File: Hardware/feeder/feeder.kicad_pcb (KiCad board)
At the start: 2 copper layers, 8 parts, among them J1 Conn_01x02, Q1 BUZ11

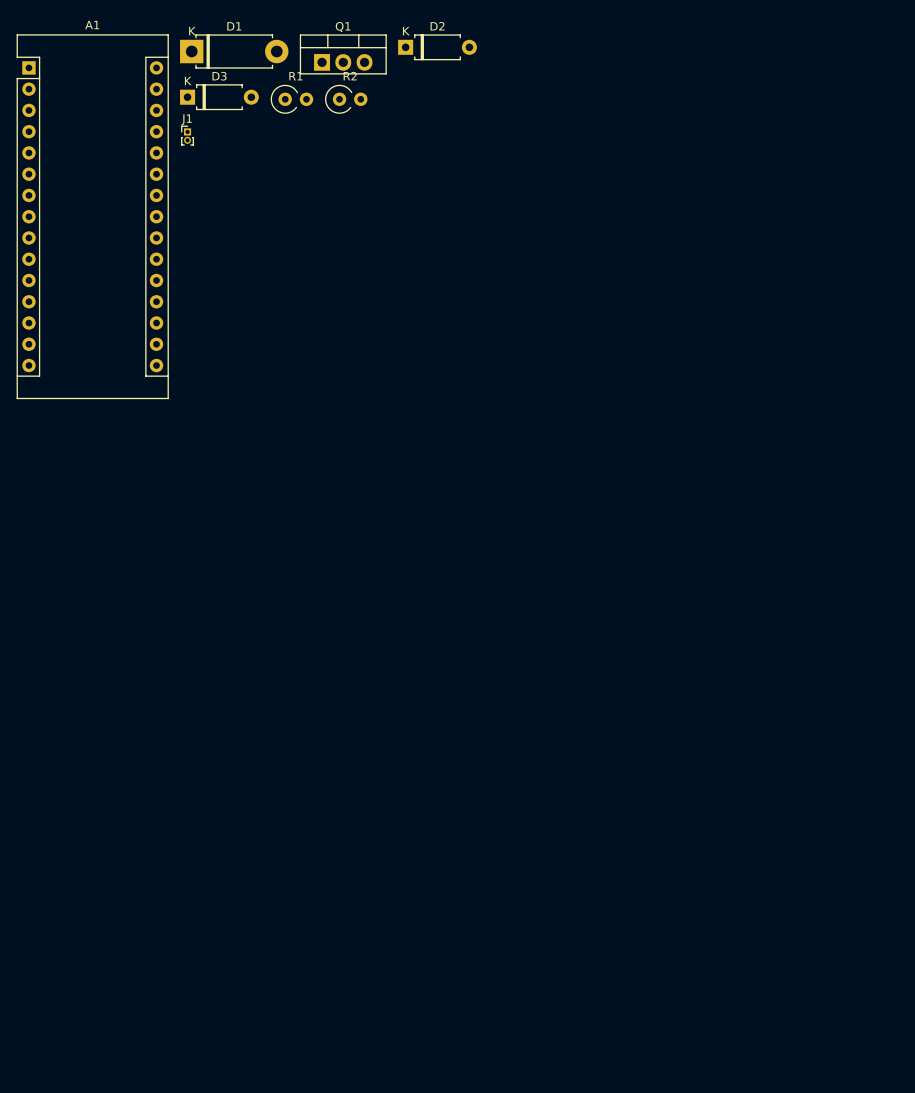
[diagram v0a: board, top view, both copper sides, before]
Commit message: Updated hardware schematics and layout
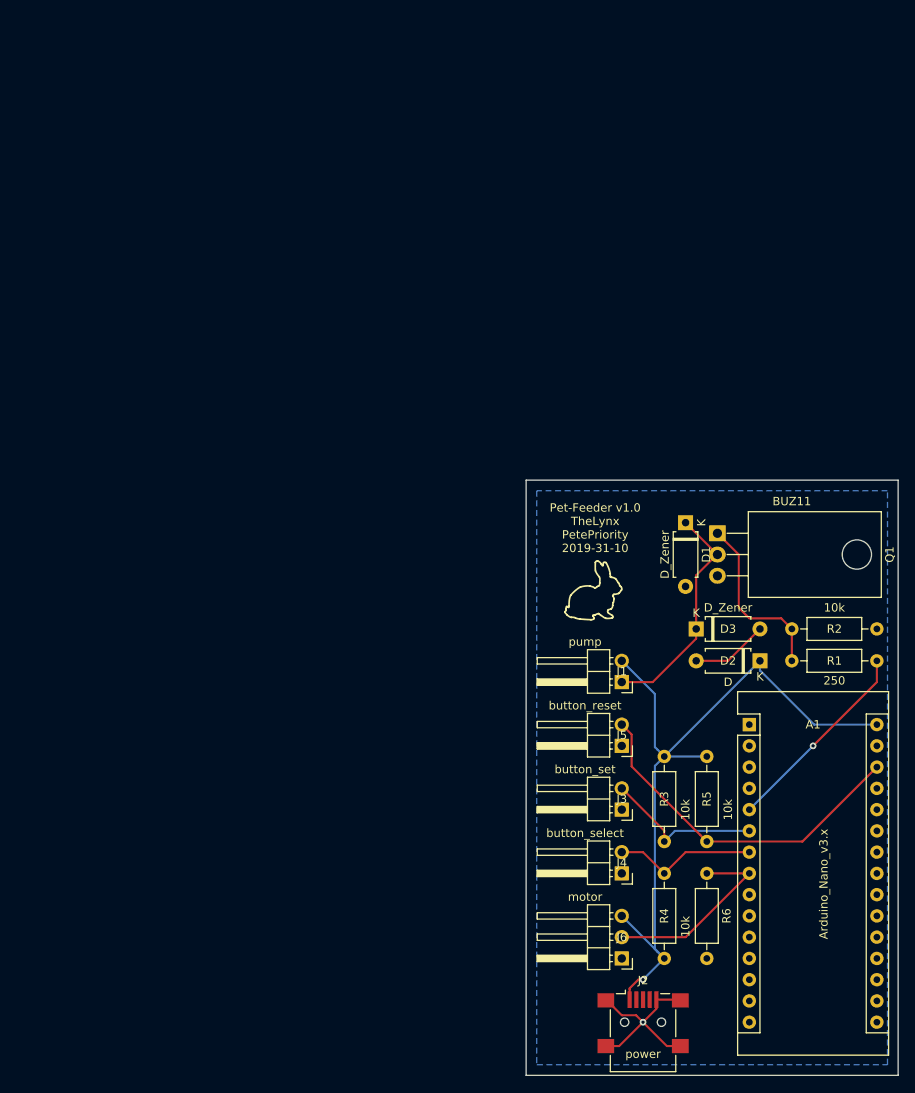
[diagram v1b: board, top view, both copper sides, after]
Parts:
- added J2: power, Connector_USB:USB_Mini-B_Lumberg_2486_01_Horizontal, F.Cu at (127.0, 141.0)
- added J3: button_set, Connector_PinHeader_2.54mm:PinHeader_1x02_P2.54mm_Horizontal, F.Cu at (124.5, 115.6)
- added J4: button_select, Connector_PinHeader_2.54mm:PinHeader_1x02_P2.54mm_Horizontal, F.Cu at (124.5, 123.2)
- added J5: button_reset, Connector_PinHeader_2.54mm:PinHeader_1x02_P2.54mm_Horizontal, F.Cu at (124.5, 108.0)
- added J6: motor, Connector_PinHeader_2.54mm:PinHeader_1x03_P2.54mm_Horizontal, F.Cu at (124.5, 133.3)
- added R3: 10k, Resistor_THT:R_Axial_DIN0207_L6.3mm_D2.5mm_P10.16mm_Horizontal, F.Cu at (129.5, 109.2)
- added R4: 10k, Resistor_THT:R_Axial_DIN0207_L6.3mm_D2.5mm_P10.16mm_Horizontal, F.Cu at (129.5, 133.3)
- added R5: 10k, Resistor_THT:R_Axial_DIN0207_L6.3mm_D2.5mm_P10.16mm_Horizontal, F.Cu at (134.6, 109.2)
- added R6: 10k, Resistor_THT:R_Axial_DIN0207_L6.3mm_D2.5mm_P10.16mm_Horizontal, F.Cu at (134.6, 123.2)
- D1: footprint Diode_THT:D_5W_P10.16mm_Horizontal -> Diode_THT:D_A-405_P7.62mm_Horizontal
- J1: value Conn_01x02 -> pump; footprint Connector_PinHeader_1.00mm:PinHeader_1x02_P1.00mm_Vertical -> Connector_PinHeader_2.54mm:PinHeader_1x02_P2.54mm_Horizontal
- Q1: footprint Package_TO_SOT_THT:TO-220-3_Vertical -> Package_TO_SOT_THT:TO-220-3_Horizontal_TabDown
- R1: value R -> 250; footprint Resistor_THT:R_Axial_DIN0309_L9.0mm_D3.2mm_P2.54mm_Vertical -> Resistor_THT:R_Axial_DIN0207_L6.3mm_D2.5mm_P10.16mm_Horizontal
- R2: value R -> 10k; footprint Resistor_THT:R_Axial_DIN0309_L9.0mm_D3.2mm_P2.54mm_Vertical -> Resistor_THT:R_Axial_DIN0207_L6.3mm_D2.5mm_P10.16mm_Horizontal
- moved A1 116.5 mm to (139.7, 105.4)
- moved R1 90.4 mm to (144.8, 97.8)
- moved D3 87.9 mm to (133.3, 94.0)
- moved D2 84.7 mm to (141.0, 97.8), turned to 180 degrees
- moved J1 83.7 mm to (124.5, 100.3), turned to 180 degrees
- moved R2 83.2 mm to (144.8, 94.0)
- moved D1 81.6 mm to (132.1, 81.3), turned to 270 degrees
- moved Q1 73.5 mm to (135.9, 82.5), turned to 270 degrees
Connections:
- A1 pad 28: Net-(A1-Pad28) -> /signal_button_reset
- A1 pad 5: /signal_motor -> /signal_pump
- A1 pad 6: Net-(A1-Pad6) -> /signal_button_set
- A1 pad 7: Net-(A1-Pad7) -> /signal_button_select
- A1 pad 8: Net-(A1-Pad8) -> /signal_motor
- R1 pad 2: /signal_motor -> /signal_pump
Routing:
- net +5V: track 0.00 -> 91.8 mm, vias 0 -> 1
- net /signal_button_reset: track 0.00 -> 42.2 mm
- net Net-(D1-Pad1): track 0.00 -> 27.6 mm
- net /signal_pump: track 0.00 -> 24.1 mm, vias 0 -> 1
- net /signal_motor: track 0.00 -> 23.5 mm
- net GND: track 0.00 -> 23.0 mm, vias 0 -> 1
- net Net-(Q1-Pad1): track 0.00 -> 21.2 mm
- net /signal_button_set: track 0.00 -> 19.1 mm
- net /signal_button_select: track 0.00 -> 17.3 mm
- net Net-(D2-Pad2): track 0.00 -> 9.20 mm
- added copper zone on B.Cu, net GND
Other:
- board outline added: 44.4 x 71.1 mm
- board text added: "Pet-Feeder v1.0 TheLynx PetePriority 2019-31-10"
